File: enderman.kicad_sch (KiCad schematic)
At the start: 24 parts, among them U1 4030, U2 LM556

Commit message: xor routing
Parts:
- added SW1: SW_SPDT, Button_Switch_SMD:SW_SPDT_PCM12, symbol Switch:SW_SPDT
- C1: value 1u -> 2u2; LCSC C15849 -> (none)
- JP1: footprint (none) -> Jumper:SolderJumper-2_P1.3mm_Open_RoundedPad1.0x1.5mm
- renumbered BT3 to BT2, BT2 to BT3
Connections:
- net +6V: now also D1.2 (A), D2.2 (A), U1.6, SW1.1 (A); no longer BT3.1 (+), R5.2, R6.2, U1.2
- net at R5.1: now also U1.12, U1.3, U1.5, U1.8; no longer D1.2 (A)
- net at D2.1 (K): now also R6.2; no longer U1.10
- net at R6.1: now also U1.10; no longer D2.2 (A)
- net at U2.9 (Q): now also U1.2; no longer U1.6
- net at JP1.1 (A): now also U1.4; no longer U1.3
- net at U2.5 (Q): now also U1.1; no longer U1.5
- new net: D1.1 (K), R5.2
- new net: BT3.1 (+), SW1.2 (B)
- no-connect marks 2 -> 3
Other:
- moved on the sheet: D1, D2, R5, R6

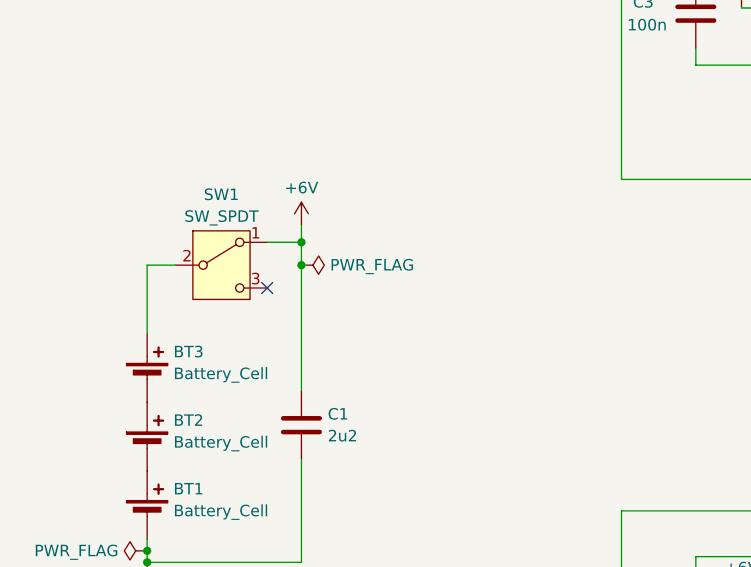
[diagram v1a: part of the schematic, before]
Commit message: routed xor version with better placement of switch
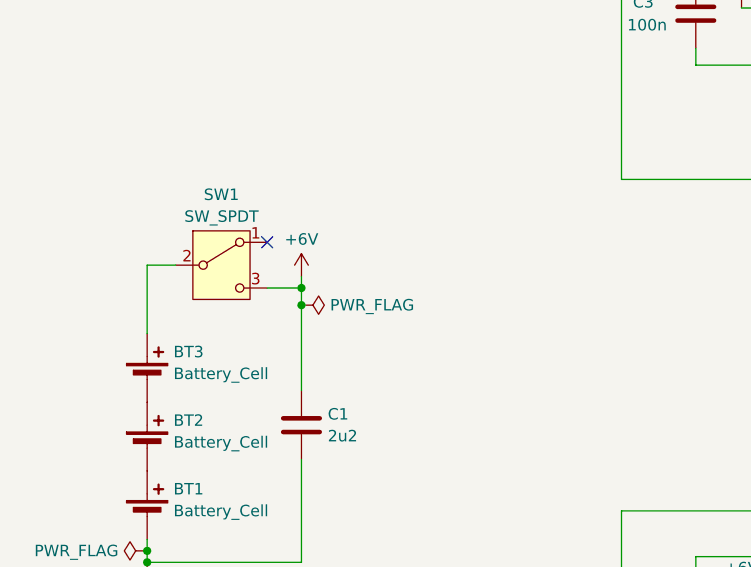
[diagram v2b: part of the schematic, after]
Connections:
- net +6V: now also SW1.3 (C); no longer SW1.1 (A)
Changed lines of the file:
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@@
   (junction (at 132.715 57.15) (diameter 0) (color 0 0 0 0)
   )
-  (junction (at 47.625 76.2) (diameter 0) (color 0 0 0 0)
-  )
-  (junction (at 47.625 78.74) (diameter 0) (color 0 0 0 0)
+  (junction (at 47.625 83.185) (diameter 0) (color 0 0 0 0)
   )
   (junction (at 111.76 56.515) (diameter 0) (color 0 0 0 0)
   )
+  (junction (at 47.625 81.28) (diameter 0) (color 0 0 0 0)
+  )
   (junction (at 184.15 37.465) (diameter 0) (color 0 0 0 0)
   )
-  (no_connect (at 43.815 81.28))
+  (no_connect (at 43.815 76.2))
   (no_connect (at 26.67 183.515))
   (no_connect (at 43.815 183.515))
@@
     (stroke (width 0) (type default))
   )
+  (wire (pts (xy 43.815 81.28) (xy 47.625 81.28))
+    (stroke (width 0) (type default))
+  )
   (wire (pts (xy 150.495 139.7) (xy 156.845 139.7))
     (stroke (width 0) (type default))
@@
     (stroke (width 0) (type default))
   )
-  (wire (pts (xy 47.625 78.74) (xy 47.625 92.71))
-    (stroke (width 0) (type default))
-  )
   (wire (pts (xy 111.76 56.515) (xy 111.76 57.15))
     (stroke (width 0) (type default))
@@
     (stroke (width 0) (type default))
   )
-  (wire (pts (xy 47.625 76.2) (xy 47.625 78.74))
+  (wire (pts (xy 47.625 80.01) (xy 47.625 81.28))
     (stroke (width 0) (type default))
   )
@@
     (stroke (width 0) (type default))
   )
-  (wire (pts (xy 47.625 74.295) (xy 47.625 76.2))
-    (stroke (width 0) (type default))
-  )
   (wire (pts (xy 196.85 113.665) (xy 196.85 142.24))
     (stroke (width 0) (type default))
@@
     (stroke (width 0) (type default))
   )
-  (wire (pts (xy 43.815 76.2) (xy 47.625 76.2))
-    (stroke (width 0) (type default))
-  )
   (wire (pts (xy 154.94 144.78) (xy 156.845 144.78))
     (stroke (width 0) (type default))
@@
     (stroke (width 0) (type default))
   )
+  (wire (pts (xy 47.625 83.185) (xy 47.625 92.71))
+    (stroke (width 0) (type default))
+  )
   (wire (pts (xy 83.185 69.215) (xy 124.46 69.215))
     (stroke (width 0) (type default))
@@
   )
   (wire (pts (xy 132.715 111.76) (xy 132.715 113.665))
+    (stroke (width 0) (type default))
+  )
+  (wire (pts (xy 47.625 81.28) (xy 47.625 83.185))
     (stroke (width 0) (type default))
   )
@@
     (effects (font (size 1.27 1.27)) (justify left bottom))
   )
-  (symbol (lib_id "power:PWR_FLAG") (at 47.625 78.74 270) (unit 1)
-    (in_bom yes) (on_board yes) (dnp no) (fields_autoplaced)
-    (property "Reference" "#FLG01" (at 49.53 78.74 0)
-      (effects (font (size 1.27 1.27)) hide)
-    )
-    (property "Value" "PWR_FLAG" (at 50.8 78.74 90)
-      (effects (font (size 1.27 1.27)) (justify left))
-    )
-    (property "Footprint" "" (at 47.625 78.74 0)
-      (effects (font (size 1.27 1.27)) hide)
-    )
-    (property "Datasheet" "~" (at 47.625 78.74 0)
+  (symbol (lib_id "power:PWR_FLAG") (at 47.625 83.185 270) (unit 1)
+    (in_bom yes) (on_board yes) (dnp no) (fields_autoplaced)
+    (property "Reference" "#FLG01" (at 49.53 83.185 0)
+      (effects (font (size 1.27 1.27)) hide)
+    )
+    (property "Value" "PWR_FLAG" (at 50.8 83.185 90)
+      (effects (font (size 1.27 1.27)) (justify left))
+    )
+    (property "Footprint" "" (at 47.625 83.185 0)
+      (effects (font (size 1.27 1.27)) hide)
+    )
+    (property "Datasheet" "~" (at 47.625 83.185 0)
       (effects (font (size 1.27 1.27)) hide)
     )
@@
     )
   )
-  (symbol (lib_id "power:+6V") (at 47.625 74.295 0) (unit 1)
-    (in_bom yes) (on_board yes) (dnp no) (fields_autoplaced)
-    (property "Reference" "#PWR01" (at 47.625 78.105 0)
-      (effects (font (size 1.27 1.27)) hide)
-    )
-    (property "Value" "+6V" (at 47.625 70.1619 0)
-      (effects (font (size 1.27 1.27)))
-    )
-    (property "Footprint" "" (at 47.625 74.295 0)
-      (effects (font (size 1.27 1.27)) hide)
-    )
-    (property "Datasheet" "" (at 47.625 74.295 0)
-      (effects (font (size 1.27 1.27)) hide)
-    )
+  (symbol (lib_id "power:+6V") (at 47.625 80.01 0) (unit 1)
+    (in_bom yes) (on_board yes) (dnp no) (fields_autoplaced)
+    (property "Reference" "#PWR01" (at 47.625 83.82 0)
+      (effects (font (size 1.27 1.27)) hide)
+    )
+    (property "Value" "+6V" (at 47.625 75.8769 0)
+      (effects (font (size 1.27 1.27)))
+    )
+    (property "Footprint" "" (at 47.625 80.01 0)
+      (effects (font (size 1.27 1.27)) hide)
+    )
+    (property "Datasheet" "" (at 47.625 80.01 0)
+      (effects (font (size 1.27 1.27)) hide)
+    )
